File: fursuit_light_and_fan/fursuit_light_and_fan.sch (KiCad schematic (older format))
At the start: 9 parts, among them M1 Low power usage 12V Fan, SW1 Switch on battery box, SW2 Eyes LED, SW3 Cooling fan

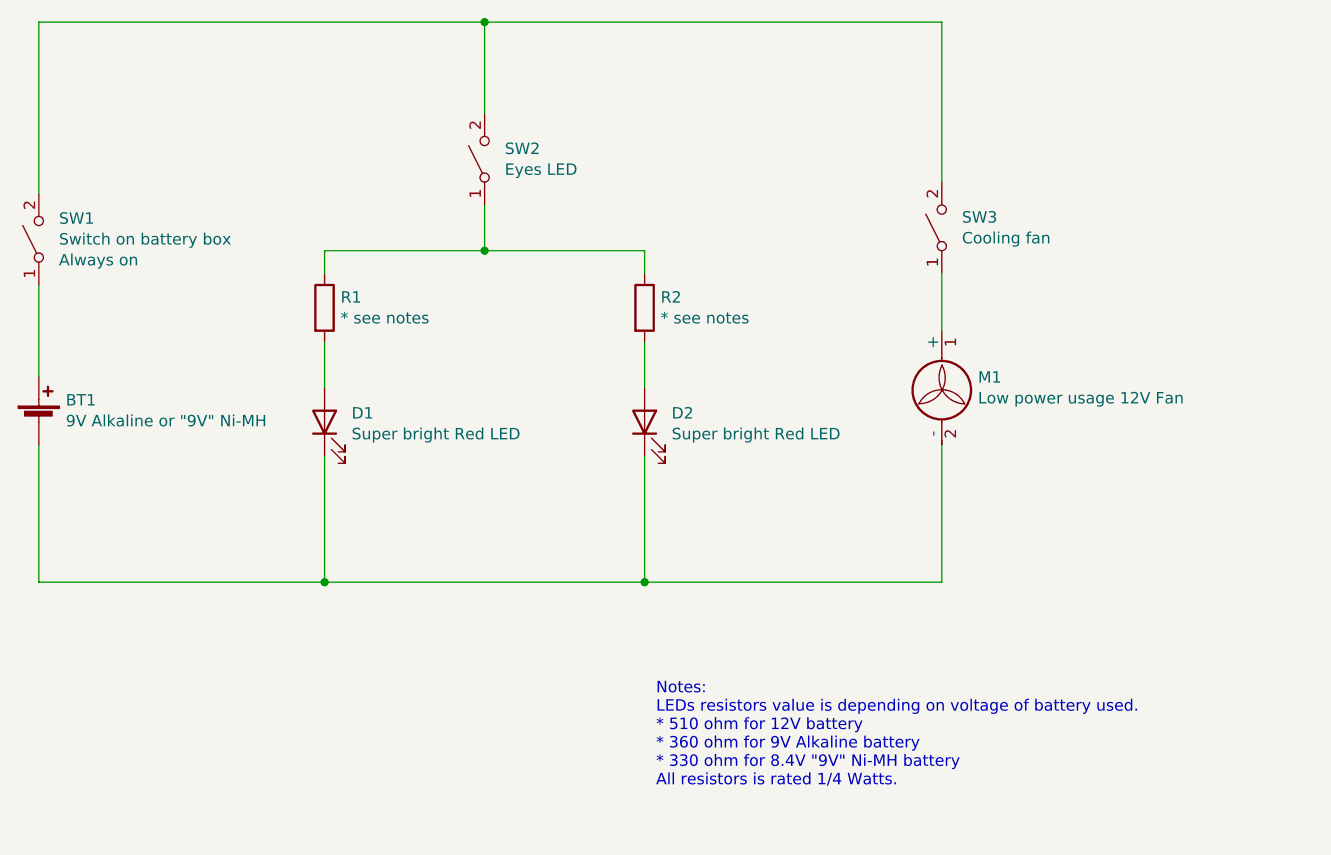
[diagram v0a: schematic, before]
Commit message: Update simple fursuit LED eyes and fan schematic.
Signed-off-by: Khralkatorrix <garuda2550@gmail.com>
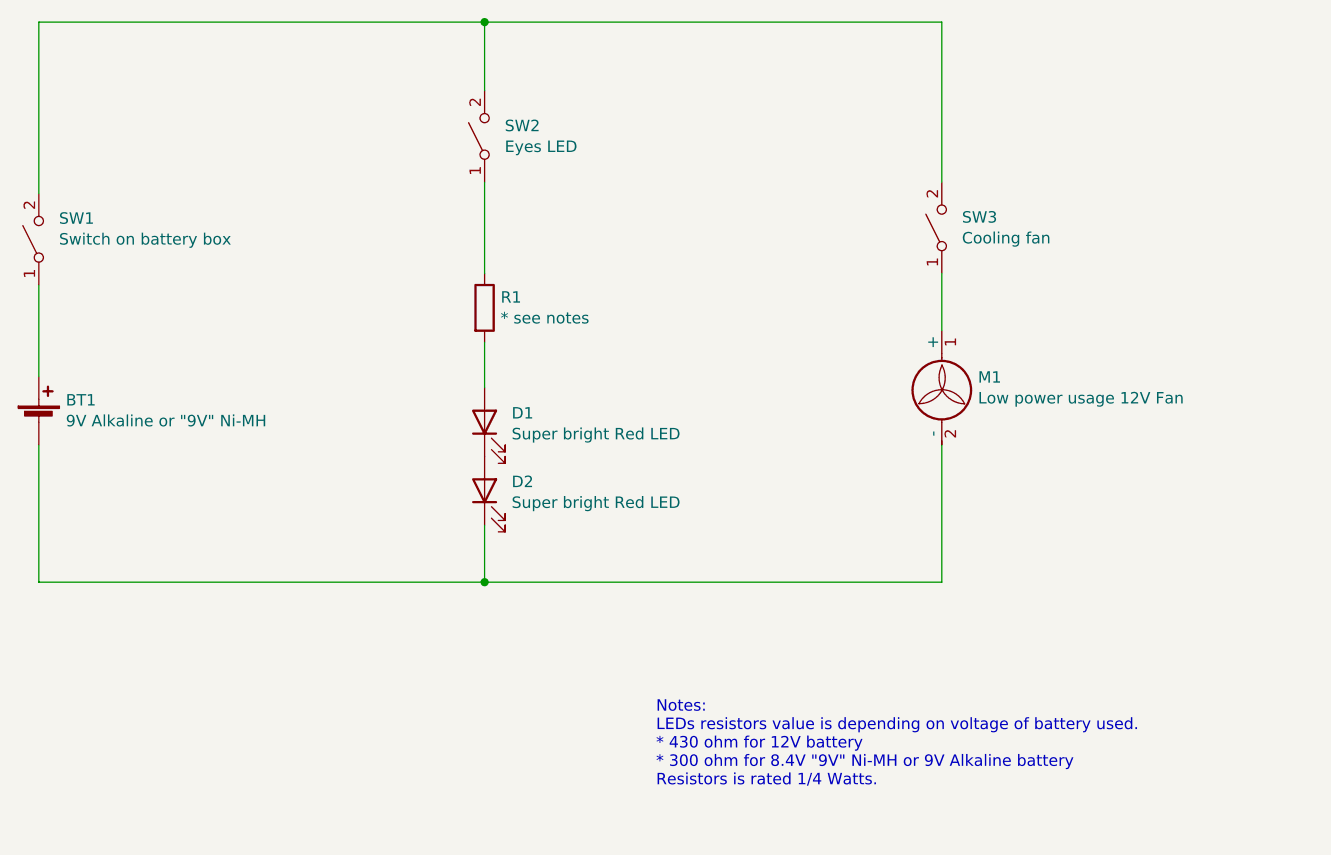
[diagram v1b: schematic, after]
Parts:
- removed R2: * see notes, symbol Device:R
- SW1: Comment Always on -> (none)
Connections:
- net at BT1.2 (-), D2.1 (K), M1.2 (-): no longer D1.1 (K)
- net at D2.2 (A): now also D1.1 (K)
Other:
- note added: "Notes:\nLEDs resistors value is depending on voltage of battery used.\n* 430 ohm for 12V battery\n* 300 ohm for 8.4V "9V" Ni-MH or 9V Alkaline battery\nResistors is rated 1/4 Watts."
- note removed: "Notes:\nLEDs resistors value is depending on voltage of battery used.\n* 510 ohm for 12V battery\n* 360 ohm for 9V Alkaline battery\n* 330 ohm for 8.4V "9V" Ni-MH battery\nAll resistors is rated 1/4 Watts."
- moved on the sheet: D1, D2, R1
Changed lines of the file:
@@
 	1    0    0    -1
-$EndComp
-$Comp
-L Switch:SW_SPST SW1
-U 1 1 5FCE7281
-P 4250 3800
-F 0 "SW1" V 4341 3712 50  0000 R CNN
-F 1 "Switch on battery box" V 4250 3712 50  0000 R CNN
-F 2 "" H 4250 3800 50  0001 C CNN
-F 3 "~" H 4250 3800 50  0001 C CNN
-F 4 "Always on" V 4159 3712 50  0000 R CNN "Comment"
-	1    4250 3800
-	0    -1   -1   0
 $EndComp
 Wire Wire Line
@@
 $EndComp
 $Comp
-L Device:LED D1
-U 1 1 5FCF16E5
-P 5500 4600
-F 0 "D1" V 5539 4482 50  0000 R CNN
-F 1 "Super bright Red LED" V 5448 4482 50  0000 R CNN
-F 2 "" H 5500 4600 50  0001 C CNN
-F 3 "~" H 5500 4600 50  0001 C CNN
-	1    5500 4600
-	0    -1   -1   0
-$EndComp
-$Comp
-L Device:LED D2
-U 1 1 5FCF1B1B
-P 6900 4600
-F 0 "D2" V 6939 4482 50  0000 R CNN
-F 1 "Super bright Red LED" V 6848 4482 50  0000 R CNN
-F 2 "" H 6900 4600 50  0001 C CNN
-F 3 "~" H 6900 4600 50  0001 C CNN
-	1    6900 4600
-	0    -1   -1   0
-$EndComp
-$Comp
-L Device:R R1
-U 1 1 5FCF2333
-P 5500 4100
-F 0 "R1" H 5570 4146 50  0000 L CNN
-F 1 "* see notes" H 5570 4055 50  0000 L CNN
-F 2 "" V 5430 4100 50  0001 C CNN
-F 3 "~" H 5500 4100 50  0001 C CNN
-	1    5500 4100
-	1    0    0    -1
-$EndComp
-$Comp
-L Device:R R2
-U 1 1 5FCF28BA
-P 6900 4100
-F 0 "R2" H 6970 4146 50  0000 L CNN
-F 1 "* see notes" H 6970 4055 50  0000 L CNN
-F 2 "" V 6830 4100 50  0001 C CNN
-F 3 "~" H 6900 4100 50  0001 C CNN
-	1    6900 4100
-	1    0    0    -1
-$EndComp
-Wire Wire Line
-	5500 4250 5500 4450
-Wire Wire Line
-	6900 4250 6900 4450
-$Comp
 L Switch:SW_SPST SW3
 U 1 1 5FD0AC5E
@@
 	0    -1   -1   0
 $EndComp
-$Comp
-L Switch:SW_SPST SW2
-U 1 1 5FD0B823
-P 6200 3450
-F 0 "SW2" V 6246 3362 50  0000 R CNN
-F 1 "Eyes LED" V 6155 3362 50  0000 R CNN
-F 2 "" H 6200 3450 50  0001 C CNN
-F 3 "~" H 6200 3450 50  0001 C CNN
-	1    6200 3450
-	0    -1   -1   0
-$EndComp
-Wire Wire Line
-	6900 3950 6900 3850
-Wire Wire Line
-	5500 3850 5500 3950
-Wire Wire Line
-	6200 3650 6200 3850
 Wire Wire Line
 	4250 4700 4250 5300
 Wire Wire Line
-	4250 5300 5500 5300
-Wire Wire Line
 	8200 5300 8200 4700
-Wire Wire Line
-	5500 4750 5500 5300
-Wire Wire Line
-	6900 4750 6900 5300
 Wire Wire Line
 	8200 3950 8200 4200
@@
 	4250 3600 4250 2850
 Wire Wire Line
+	8200 2850 8200 3550
+$Comp
+L Switch:SW_SPST SW1
+U 1 1 5FCE7281
+P 4250 3800
+F 0 "SW1" V 4341 3712 50  0000 R CNN
+F 1 "Switch on battery box" V 4250 3712 50  0000 R CNN
+F 2 "" H 4250 3800 50  0001 C CNN
+F 3 "~" H 4250 3800 50  0001 C CNN
+F 4 "" V 4159 3712 50  0001 R CNN "Comment"
+	1    4250 3800
+	0    -1   -1   0
+$EndComp
+$Comp
+L Device:LED D1
+U 1 1 5FCF16E5
+P 6200 4600
+F 0 "D1" V 6239 4482 50  0000 R CNN
+F 1 "Super bright Red LED" V 6148 4482 50  0000 R CNN
+F 2 "" H 6200 4600 50  0001 C CNN
+F 3 "~" H 6200 4600 50  0001 C CNN
+	1    6200 4600
+	0    -1   -1   0
+$EndComp
+$Comp
+L Device:LED D2
+U 1 1 5FCF1B1B
+P 6200 4900
+F 0 "D2" V 6239 4782 50  0000 R CNN
+F 1 "Super bright Red LED" V 6148 4782 50  0000 R CNN
+F 2 "" H 6200 4900 50  0001 C CNN
+F 3 "~" H 6200 4900 50  0001 C CNN
+	1    6200 4900
+	0    -1   -1   0
+$EndComp
+$Comp
+L Device:R R1
+U 1 1 5FCF2333
+P 6200 4100
+F 0 "R1" H 6270 4146 50  0000 L CNN
+F 1 "* see notes" H 6270 4055 50  0000 L CNN
+F 2 "" V 6130 4100 50  0001 C CNN
+F 3 "~" H 6200 4100 50  0001 C CNN
+	1    6200 4100
+	1    0    0    -1
+$EndComp
+Wire Wire Line
+	6200 4250 6200 4450
+Wire Wire Line
+	6200 5050 6200 5300
+Wire Wire Line
+	4250 5300 6200 5300
+Wire Wire Line
+	6200 5300 8200 5300
+Connection ~ 6200 5300
+Text Notes 6950 6200 0    50   ~ 0
+Notes:\nLEDs resistors value is depending on voltage of battery used.\n* 430 ohm for 12V battery\n* 300 ohm for 8.4V "9V" Ni-MH or 9V Alkaline battery\nResistors is rated 1/4 Watts.
+$Comp
+L Switch:SW_SPST SW2
+U 1 1 60958769
+P 6200 3350
+F 0 "SW2" V 6246 3262 50  0000 R CNN
+F 1 "Eyes LED" V 6155 3262 50  0000 R CNN
+F 2 "" H 6200 3350 50  0001 C CNN
+F 3 "~" H 6200 3350 50  0001 C CNN
+	1    6200 3350
+	0    -1   -1   0
+$EndComp
+Wire Wire Line
 	4250 2850 6200 2850
 Wire Wire Line
-	8200 2850 8200 3550
+	6200 3550 6200 3950
 Wire Wire Line
-	6200 3250 6200 2850
+	6200 3150 6200 2850
 Connection ~ 6200 2850
-Connection ~ 5500 5300
-Connection ~ 6900 5300
-Wire Wire Line
-	5500 5300 6900 5300
 Wire Wire Line
 	6200 2850 8200 2850
-Wire Wire Line
-	6900 5300 8200 5300
-Wire Wire Line
-	5500 3850 6200 3850
-Connection ~ 6200 3850
-Wire Wire Line
-	6200 3850 6900 3850
-Text Notes 6950 6200 0    50   ~ 0
-Notes:\nLEDs resistors value is depending on voltage of battery used.\n* 510 ohm for 12V battery\n* 360 ohm for 9V Alkaline battery\n* 330 ohm for 8.4V "9V" Ni-MH battery\nAll resistors is rated 1/4 Watts.
 $EndSCHEMATC

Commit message: Update simple fursuit LED eyes and fan schematic.
Signed-off-by: Khralkatorrix <garuda2550@gmail.com>
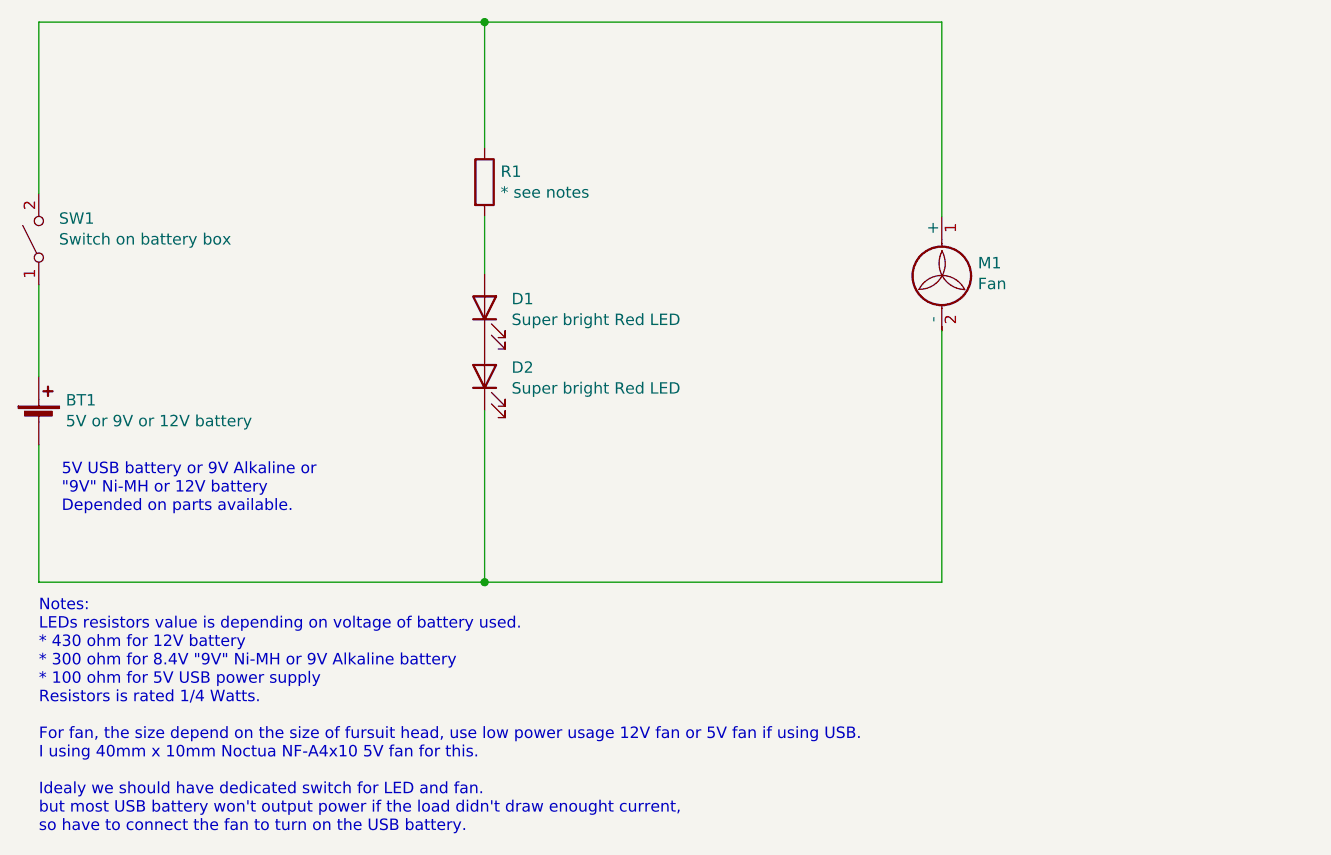
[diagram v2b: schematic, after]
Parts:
- removed SW2: Eyes LED, symbol Switch:SW_SPST
- removed SW3: Cooling fan, symbol Switch:SW_SPST
- BT1: value 9V Alkaline or \"9V\" Ni-MH -> 5V or 9V or 12V battery
- M1: value Low power usage 12V Fan -> Fan
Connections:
- net at SW1.2 (B): now also M1.1 (+), R1.1
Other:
- note added: "5V USB battery or 9V Alkaline or\n"9V" Ni-MH or 12V battery\nDepended on parts available."
- note added: "Notes:\nLEDs resistors value is depending on voltage of battery used.\n* 430 ohm for 12V battery\n* 300 ohm for 8.4V "9V" Ni-MH or 9V Alkaline battery\n* 100 ohm for 5V USB power supply\nResistors is rated 1/4 Watts.\n\nFor fan, the size depend on the size of fursuit head, use low power usage 12V fan or 5V fan if using USB.\nI using 40mm x 10mm Noctua NF-A4x10 5V fan for this.\n\nIdealy we should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"
- note removed: "Notes:\nLEDs resistors value is depending on voltage of battery used.\n* 430 ohm for 12V battery\n* 300 ohm for 8.4V "9V" Ni-MH or 9V Alkaline battery\nResistors is rated 1/4 Watts."
- moved on the sheet: D1, D2, M1, R1
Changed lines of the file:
@@
 P 4250 4600
 F 0 "BT1" H 4368 4696 50  0000 L CNN
-F 1 "9V Alkaline or \"9V\" Ni-MH" H 4368 4605 50  0000 L CNN
+F 1 "5V or 9V or 12V battery" H 4368 4605 50  0000 L CNN
 F 2 "" V 4250 4660 50  0001 C CNN
 F 3 "~" V 4250 4660 50  0001 C CNN
@@
 L Motor:Fan M1
 U 1 1 5FCEF87D
-P 8200 4500
-F 0 "M1" H 8358 4596 50  0000 L CNN
-F 1 "Low power usage 12V Fan" H 8358 4505 50  0000 L CNN
-F 2 "" H 8200 4510 50  0001 C CNN
-F 3 "~" H 8200 4510 50  0001 C CNN
-	1    8200 4500
+P 8200 4000
+F 0 "M1" H 8358 4096 50  0000 L CNN
+F 1 "Fan" H 8358 4005 50  0000 L CNN
+F 2 "" H 8200 4010 50  0001 C CNN
+F 3 "~" H 8200 4010 50  0001 C CNN
+	1    8200 4000
 	1    0    0    -1
-$EndComp
-$Comp
-L Switch:SW_SPST SW3
-U 1 1 5FD0AC5E
-P 8200 3750
-F 0 "SW3" V 8246 3662 50  0000 R CNN
-F 1 "Cooling fan" V 8155 3662 50  0000 R CNN
-F 2 "" H 8200 3750 50  0001 C CNN
-F 3 "~" H 8200 3750 50  0001 C CNN
-	1    8200 3750
-	0    -1   -1   0
 $EndComp
 Wire Wire Line
 	4250 4700 4250 5300
 Wire Wire Line
-	8200 5300 8200 4700
-Wire Wire Line
-	8200 3950 8200 4200
+	8200 5300 8200 4200
 Wire Wire Line
 	4250 3600 4250 2850
 Wire Wire Line
-	8200 2850 8200 3550
+	8200 3700 8200 2850
 $Comp
 L Switch:SW_SPST SW1
@@
 	0    -1   -1   0
 $EndComp
+Text Notes 4250 6400 0    50   ~ 0
+Notes:\nLEDs resistors value is depending on voltage of battery used.\n* 430 ohm for 12V battery\n* 300 ohm for 8.4V "9V" Ni-MH or 9V Alkaline battery\n* 100 ohm for 5V USB power supply\nResistors is rated 1/4 Watts.\n\nFor fan, the size depend on the size of fursuit head, use low power usage 12V fan or 5V fan if using USB.\nI using 40mm x 10mm Noctua NF-A4x10 5V fan for this.\n\nIdealy we should have dedicated switch for LED and fan.\nbut most USB battery won't output power if the load didn't draw enought current,\nso have to connect the fan to turn on the USB battery.
+$Comp
+L Device:R R1
+U 1 1 5FCF2333
+P 6200 3550
+F 0 "R1" H 6270 3596 50  0000 L CNN
+F 1 "* see notes" H 6270 3505 50  0000 L CNN
+F 2 "" V 6130 3550 50  0001 C CNN
+F 3 "~" H 6200 3550 50  0001 C CNN
+	1    6200 3550
+	1    0    0    -1
+$EndComp
+Wire Wire Line
+	6200 4550 6200 5300
+$Comp
+L Device:LED D2
+U 1 1 5FCF1B1B
+P 6200 4400
+F 0 "D2" V 6239 4282 50  0000 R CNN
+F 1 "Super bright Red LED" V 6148 4282 50  0000 R CNN
+F 2 "" H 6200 4400 50  0001 C CNN
+F 3 "~" H 6200 4400 50  0001 C CNN
+	1    6200 4400
+	0    -1   -1   0
+$EndComp
 $Comp
 L Device:LED D1
 U 1 1 5FCF16E5
-P 6200 4600
-F 0 "D1" V 6239 4482 50  0000 R CNN
-F 1 "Super bright Red LED" V 6148 4482 50  0000 R CNN
-F 2 "" H 6200 4600 50  0001 C CNN
-F 3 "~" H 6200 4600 50  0001 C CNN
-	1    6200 4600
-	0    -1   -1   0
-$EndComp
-$Comp
-L Device:LED D2
-U 1 1 5FCF1B1B
-P 6200 4900
-F 0 "D2" V 6239 4782 50  0000 R CNN
-F 1 "Super bright Red LED" V 6148 4782 50  0000 R CNN
-F 2 "" H 6200 4900 50  0001 C CNN
-F 3 "~" H 6200 4900 50  0001 C CNN
-	1    6200 4900
-	0    -1   -1   0
-$EndComp
-$Comp
-L Device:R R1
-U 1 1 5FCF2333
 P 6200 4100
-F 0 "R1" H 6270 4146 50  0000 L CNN
-F 1 "* see notes" H 6270 4055 50  0000 L CNN
-F 2 "" V 6130 4100 50  0001 C CNN
+F 0 "D1" V 6239 3982 50  0000 R CNN
+F 1 "Super bright Red LED" V 6148 3982 50  0000 R CNN
+F 2 "" H 6200 4100 50  0001 C CNN
 F 3 "~" H 6200 4100 50  0001 C CNN
 	1    6200 4100
-	1    0    0    -1
-$EndComp
-Wire Wire Line
-	6200 4250 6200 4450
-Wire Wire Line
-	6200 5050 6200 5300
-Wire Wire Line
-	4250 5300 6200 5300
-Wire Wire Line
-	6200 5300 8200 5300
-Connection ~ 6200 5300
-Text Notes 6950 6200 0    50   ~ 0
-Notes:\nLEDs resistors value is depending on voltage of battery used.\n* 430 ohm for 12V battery\n* 300 ohm for 8.4V "9V" Ni-MH or 9V Alkaline battery\nResistors is rated 1/4 Watts.
-$Comp
-L Switch:SW_SPST SW2
-U 1 1 60958769
-P 6200 3350
-F 0 "SW2" V 6246 3262 50  0000 R CNN
-F 1 "Eyes LED" V 6155 3262 50  0000 R CNN
-F 2 "" H 6200 3350 50  0001 C CNN
-F 3 "~" H 6200 3350 50  0001 C CNN
-	1    6200 3350
 	0    -1   -1   0
 $EndComp
@@
 	4250 2850 6200 2850
 Wire Wire Line
-	6200 3550 6200 3950
+	4250 5300 6200 5300
+Connection ~ 6200 5300
 Wire Wire Line
-	6200 3150 6200 2850
+	6200 5300 8200 5300
+Wire Wire Line
+	6200 3950 6200 3700
+Wire Wire Line
+	6200 3400 6200 2850
 Connection ~ 6200 2850
 Wire Wire Line
 	6200 2850 8200 2850
+Text Notes 4350 5000 0    50   ~ 0
+5V USB battery or 9V Alkaline or\n"9V" Ni-MH or 12V battery\nDepended on parts available.
 $EndSCHEMATC
